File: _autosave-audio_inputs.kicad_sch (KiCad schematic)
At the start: 14 parts, among them J2 PLR237/T10BK, U4 DIR9001PW

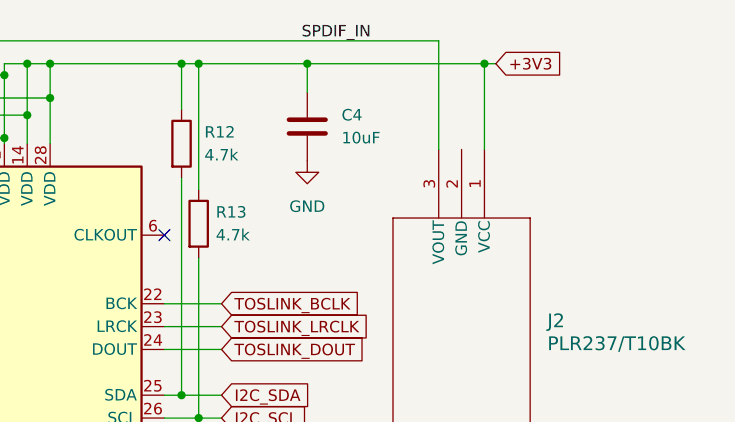
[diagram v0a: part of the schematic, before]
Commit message: Added symbol and footprint for PLR237/T10BK Toslink
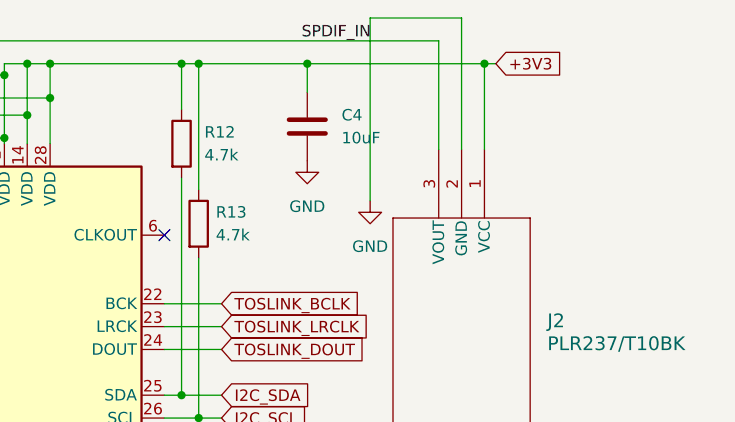
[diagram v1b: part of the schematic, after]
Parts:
- J2: footprint PLR237/T10BK_EVE -> Connector_Audio:PLR237-T10BK
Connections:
- net GND: now also J2.2 (GND)
